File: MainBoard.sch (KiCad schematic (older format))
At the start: 36 parts, among them J1 Qwiic connector, J2 Qwiic connector, J25 Conn_01x02_Female, J3 Conn_01x03_Male, J4 Conn_01x03_Male, J5 Conn_01x03_Male, J6 Conn_01x03_Male, J7 Micro_SD_Card, U1 PCA9685BS

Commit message: Ready to order
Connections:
- net GND: now also U1.22 (EXTCLK)
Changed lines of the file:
@@
 Wire Notes Line
 	500  4000 11250 4000
+$Comp
+L power:GND #PWR0216
+U 1 1 6037187A
+P 5300 1700
+F 0 "#PWR0216" H 5300 1450 50  0001 C CNN
+F 1 "GND" V 5305 1572 50  0000 R CNN
+F 2 "" H 5300 1700 50  0001 C CNN
+F 3 "" H 5300 1700 50  0001 C CNN
+	1    5300 1700
+	0    1    1    0
+$EndComp
 $EndSCHEMATC

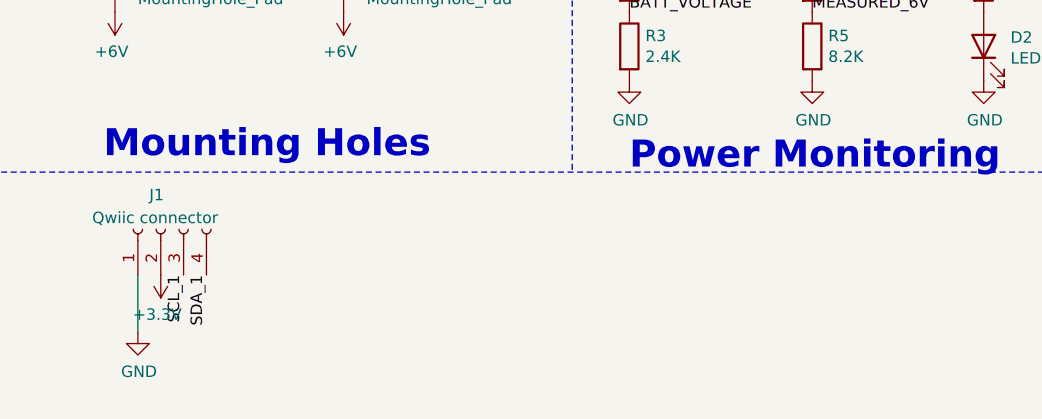
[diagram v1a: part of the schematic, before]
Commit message: ordered version with foot connecotrs
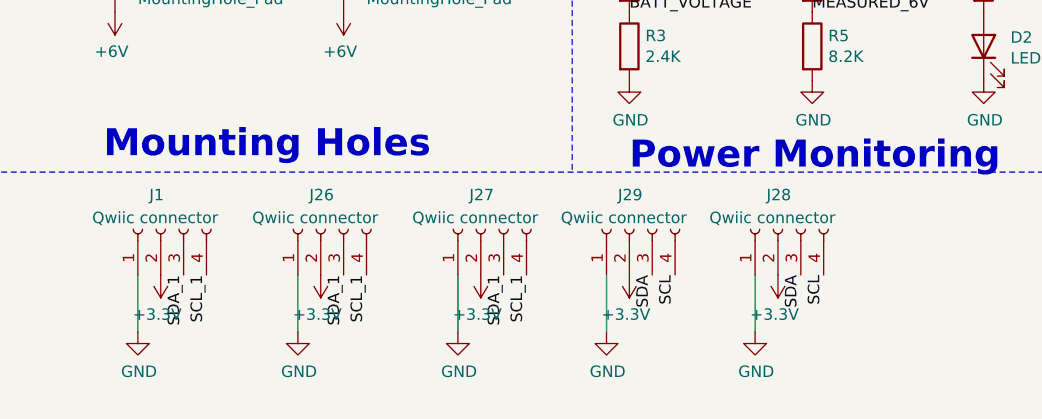
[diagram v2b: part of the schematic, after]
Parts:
- added J26, J27, J28, J29: Qwiic connector, Connector_JST:JST_SH_BM04B-SRSS-TB_1x04-1MP_P1.00mm_Vertical, symbol Connector:Conn_01x04_Female
- J1, J2: footprint Connector_JST:JST_SH_SM04B-SRSS-TB_1x04-1MP_P1.00mm_Horizontal -> Connector_JST:JST_SH_BM04B-SRSS-TB_1x04-1MP_P1.00mm_Vertical
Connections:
- net +3V3: now also J26.2 (Pin_2), J27.2 (Pin_2), J28.2 (Pin_2), J29.2 (Pin_2)
- net GND: now also J26.1 (Pin_1), J27.1 (Pin_1), J28.1 (Pin_1), J29.1 (Pin_1)
- net SCL: now also J28.4 (Pin_4), J29.4 (Pin_4)
- net SCL_1: now also J1.4 (Pin_4), J26.4 (Pin_4), J27.4 (Pin_4); no longer J1.3 (Pin_3)
- net SDA: now also J28.3 (Pin_3), J29.3 (Pin_3)
- net SDA_1: now also J1.3 (Pin_3), J26.3 (Pin_3), J27.3 (Pin_3); no longer J1.4 (Pin_4)
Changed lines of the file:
@@
 F 0 "J2" V 2700 4300 50  0000 R CNN
 F 1 "Qwiic connector" V 2600 4550 50  0000 R CNN
-F 2 "Connector_JST:JST_SH_SM04B-SRSS-TB_1x04-1MP_P1.00mm_Horizontal" H 2550 4250 50  0001 C CNN
+F 2 "Connector_JST:JST_SH_BM04B-SRSS-TB_1x04-1MP_P1.00mm_Vertical" H 2550 4250 50  0001 C CNN
 F 3 "~" H 2550 4250 50  0001 C CNN
 	1    2550 4250
@@
 F 0 "J1" V 1550 7150 50  0000 R CNN
 F 1 "Qwiic connector" V 1450 7400 50  0000 R CNN
-F 2 "Connector_JST:JST_SH_SM04B-SRSS-TB_1x04-1MP_P1.00mm_Horizontal" H 1400 7100 50  0001 C CNN
+F 2 "Connector_JST:JST_SH_BM04B-SRSS-TB_1x04-1MP_P1.00mm_Vertical" H 1400 7100 50  0001 C CNN
 F 3 "~" H 1400 7100 50  0001 C CNN
 	1    1400 7100
@@
 $EndComp
 Text Label 1500 7300 3    50   ~ 0
+SDA_1
+Text Label 1600 7300 3    50   ~ 0
 SCL_1
-Text Label 1600 7300 3    50   ~ 0
-SDA_1
 Wire Notes Line
 	5350 5600 5350 7850
@@
 	0    1    1    0
 $EndComp
+$Comp
+L power:GND #PWR0217
+U 1 1 601A37F1
+P 2000 7550
+F 0 "#PWR0217" H 2000 7300 50  0001 C CNN
+F 1 "GND" H 2005 7377 50  0000 C CNN
+F 2 "" H 2000 7550 50  0001 C CNN
+F 3 "" H 2000 7550 50  0001 C CNN
+	1    2000 7550
+	1    0    0    -1
+$EndComp
+Wire Wire Line
+	2000 7300 2000 7550
+$Comp
+L Connector:Conn_01x04_Female J26
+U 1 1 601A37F8
+P 2100 7100
+F 0 "J26" V 2250 7150 50  0000 R CNN
+F 1 "Qwiic connector" V 2150 7400 50  0000 R CNN
+F 2 "Connector_JST:JST_SH_BM04B-SRSS-TB_1x04-1MP_P1.00mm_Vertical" H 2100 7100 50  0001 C CNN
+F 3 "~" H 2100 7100 50  0001 C CNN
+	1    2100 7100
+	0    -1   -1   0
+$EndComp
+$Comp
+L power:+3.3V #PWR0218
+U 1 1 601A37FE
+P 2100 7300
+F 0 "#PWR0218" H 2100 7150 50  0001 C CNN
+F 1 "+3.3V" H 2115 7473 50  0000 C CNN
+F 2 "" H 2100 7300 50  0001 C CNN
+F 3 "" H 2100 7300 50  0001 C CNN
+	1    2100 7300
+	-1   0    0    1
+$EndComp
+$Comp
+L power:GND #PWR0219
+U 1 1 601A471C
+P 2700 7550
+F 0 "#PWR0219" H 2700 7300 50  0001 C CNN
+F 1 "GND" H 2705 7377 50  0000 C CNN
+F 2 "" H 2700 7550 50  0001 C CNN
+F 3 "" H 2700 7550 50  0001 C CNN
+	1    2700 7550
+	1    0    0    -1
+$EndComp
+Wire Wire Line
+	2700 7300 2700 7550
+$Comp
+L Connector:Conn_01x04_Female J27
+U 1 1 601A4723
+P 2800 7100
+F 0 "J27" V 2950 7150 50  0000 R CNN
+F 1 "Qwiic connector" V 2850 7400 50  0000 R CNN
+F 2 "Connector_JST:JST_SH_BM04B-SRSS-TB_1x04-1MP_P1.00mm_Vertical" H 2800 7100 50  0001 C CNN
+F 3 "~" H 2800 7100 50  0001 C CNN
+	1    2800 7100
+	0    -1   -1   0
+$EndComp
+$Comp
+L power:+3.3V #PWR0220
+U 1 1 601A4729
+P 2800 7300
+F 0 "#PWR0220" H 2800 7150 50  0001 C CNN
+F 1 "+3.3V" H 2815 7473 50  0000 C CNN
+F 2 "" H 2800 7300 50  0001 C CNN
+F 3 "" H 2800 7300 50  0001 C CNN
+	1    2800 7300
+	-1   0    0    1
+$EndComp
+$Comp
+L power:GND #PWR0221
+U 1 1 601A5126
+P 4000 7550
+F 0 "#PWR0221" H 4000 7300 50  0001 C CNN
+F 1 "GND" H 4005 7377 50  0000 C CNN
+F 2 "" H 4000 7550 50  0001 C CNN
+F 3 "" H 4000 7550 50  0001 C CNN
+	1    4000 7550
+	1    0    0    -1
+$EndComp
+Wire Wire Line
+	4000 7300 4000 7550
+$Comp
+L Connector:Conn_01x04_Female J28
+U 1 1 601A512D
+P 4100 7100
+F 0 "J28" V 4250 7150 50  0000 R CNN
+F 1 "Qwiic connector" V 4150 7400 50  0000 R CNN
+F 2 "Connector_JST:JST_SH_BM04B-SRSS-TB_1x04-1MP_P1.00mm_Vertical" H 4100 7100 50  0001 C CNN
+F 3 "~" H 4100 7100 50  0001 C CNN
+	1    4100 7100
+	0    -1   -1   0
+$EndComp
+$Comp
+L power:+3.3V #PWR0222
+U 1 1 601A5133
+P 4100 7300
+F 0 "#PWR0222" H 4100 7150 50  0001 C CNN
+F 1 "+3.3V" H 4115 7473 50  0000 C CNN
+F 2 "" H 4100 7300 50  0001 C CNN
+F 3 "" H 4100 7300 50  0001 C CNN
+	1    4100 7300
+	-1   0    0    1
+$EndComp
+Text Label 4300 7300 3    50   ~ 0
+SCL
+Text Label 4200 7300 3    50   ~ 0
+SDA
+Text Label 2200 7300 3    50   ~ 0
+SDA_1
+Text Label 2300 7300 3    50   ~ 0
+SCL_1
+Text Label 3000 7300 3    50   ~ 0
+SCL_1
+Text Label 2900 7300 3    50   ~ 0
+SDA_1
+$Comp
+L power:GND #PWR0223
+U 1 1 601E4042
+P 3350 7550
+F 0 "#PWR0223" H 3350 7300 50  0001 C CNN
+F 1 "GND" H 3355 7377 50  0000 C CNN
+F 2 "" H 3350 7550 50  0001 C CNN
+F 3 "" H 3350 7550 50  0001 C CNN
+	1    3350 7550
+	1    0    0    -1
+$EndComp
+Wire Wire Line
+	3350 7300 3350 7550
+$Comp
+L Connector:Conn_01x04_Female J29
+U 1 1 601E4049
+P 3450 7100
+F 0 "J29" V 3600 7150 50  0000 R CNN
+F 1 "Qwiic connector" V 3500 7400 50  0000 R CNN
+F 2 "Connector_JST:JST_SH_BM04B-SRSS-TB_1x04-1MP_P1.00mm_Vertical" H 3450 7100 50  0001 C CNN
+F 3 "~" H 3450 7100 50  0001 C CNN
+	1    3450 7100
+	0    -1   -1   0
+$EndComp
+$Comp
+L power:+3.3V #PWR0224
+U 1 1 601E404F
+P 3450 7300
+F 0 "#PWR0224" H 3450 7150 50  0001 C CNN
+F 1 "+3.3V" H 3465 7473 50  0000 C CNN
+F 2 "" H 3450 7300 50  0001 C CNN
+F 3 "" H 3450 7300 50  0001 C CNN
+	1    3450 7300
+	-1   0    0    1
+$EndComp
+Text Label 3650 7300 3    50   ~ 0
+SCL
+Text Label 3550 7300 3    50   ~ 0
+SDA
 $EndSCHEMATC
